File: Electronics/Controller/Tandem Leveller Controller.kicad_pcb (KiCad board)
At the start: 2 copper layers, 212 x 145 mm, 133 parts, among them J1 Conn_01x02, J10 CAN BUS, J11 TRACTOR BATTERY, J12 PWR SWITCH, J13 VALVE POWER, J14 TABLET 1 PWR, J15 TABLET 2 PWR, J16 SLAVE TABLET, J17 MASTER TABLET, J18 292303-7, J19 292303-7, J2 GPS SIM, J20 FRONT HEIGHT, J21 REAR HEIGHT, J23 CAN, J24 CAN BUS, J25 CAN BUS, J3 Conn_01x02, J4 Conn_01x02, J5 Conn_01x02, J6 Conn_01x02, J7 Conn_01x02, J8 Conn_01x02, J9 TERM, U1 TEENSY 4.0, U10 FT232RL, U11 FT232RL, U12 FT232RL, U13 FT232RL, U14 FT232RL, U15 FT232RL, U16 USB2517, U17 MIC2026-1YM, U2 simpleRTK2B, U3 simpleRTK2B, U4 simpleRTK2B, U5 TJA1462ATK-0Z, U6 PESD2CANFD24V-TR, U7 LM2596S-5, U8 LM2587S-ADJ/NOPB, U9 LM2587S-ADJ/NOPB, Y1 FA-238 24.0000MD30X-W5

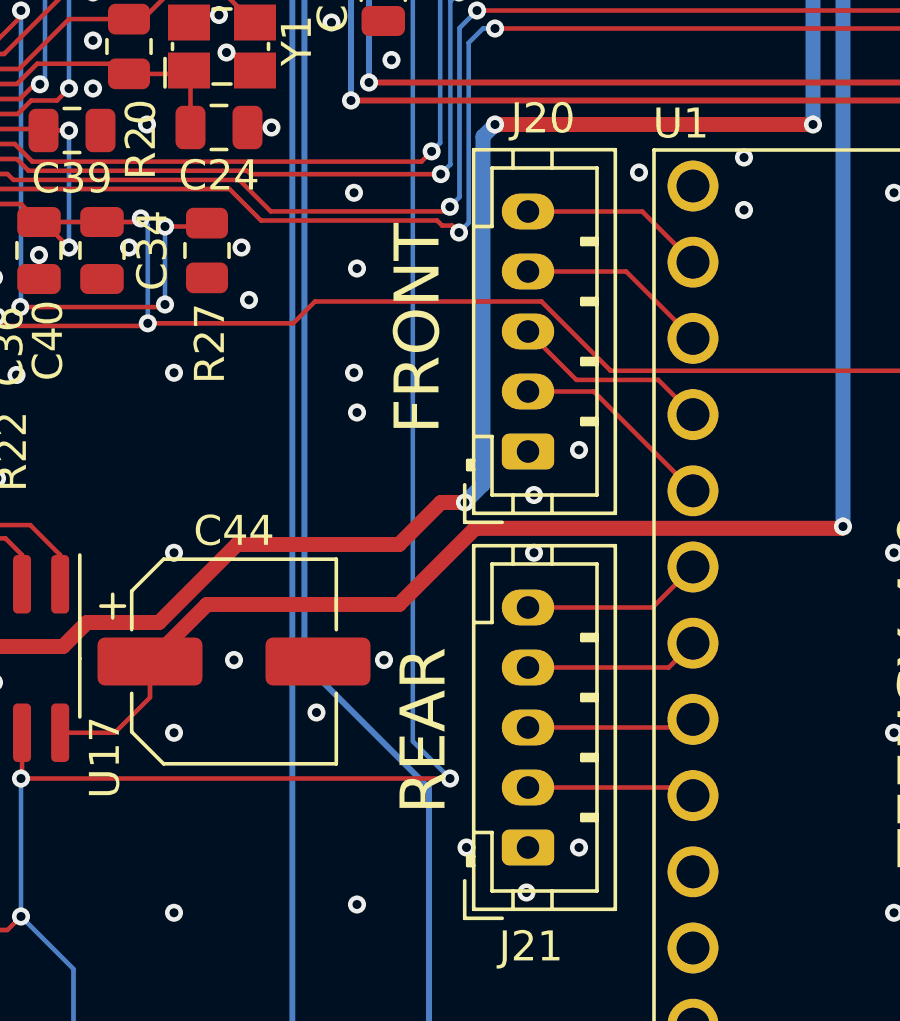
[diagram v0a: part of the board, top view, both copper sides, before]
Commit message: Renamed valve control connectors and reordered pins to match pinout of MDD10A connectors.
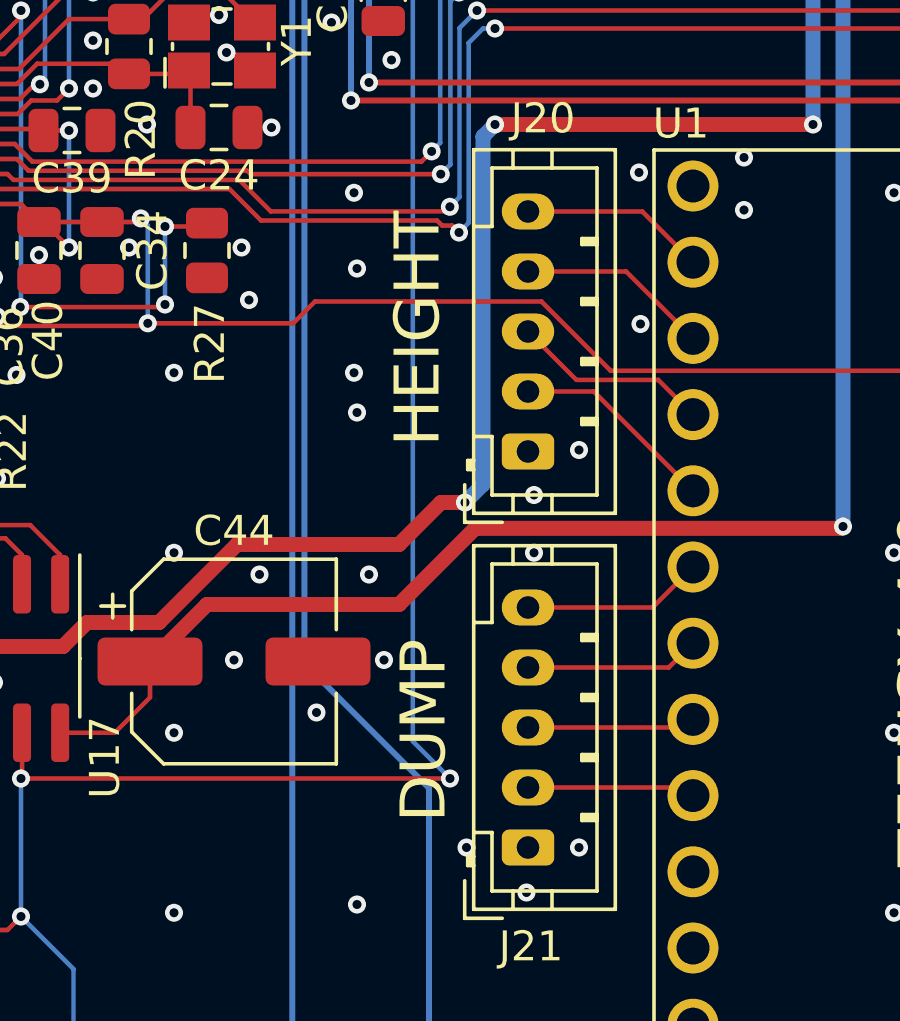
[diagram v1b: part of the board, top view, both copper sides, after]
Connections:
- net /Valve Control/FRONT_DIR1 renamed /Valve Control/FRONT_HEIGHT_PWM
- net /Valve Control/FRONT_DIR2 renamed /Valve Control/REAR_HEIGHT_PWM
- net /Valve Control/FRONT_PWM1 renamed /Valve Control/FRONT_HEIGHT_DIR
- net /Valve Control/FRONT_PWM2 renamed /Valve Control/REAR_HEIGHT_DIR
- net /Valve Control/REAR_DIR1 renamed /Valve Control/FRONT_DUMP_PWM
- net /Valve Control/REAR_DIR2 renamed /Valve Control/REAR_DUMP_PWM
- net /Valve Control/REAR_PWM1 renamed /Valve Control/FRONT_DUMP_DIR
- net /Valve Control/REAR_PWM2 renamed /Valve Control/REAR_DUMP_DIR
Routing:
- net GND: vias 858 -> 861
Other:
- board text added: "DUMP"
- board text added: "HEIGHT"
- board text removed: "FRONT"
- board text removed: "REAR"
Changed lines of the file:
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@@
   (net 63 "Net-(J19-D-)")
   (net 64 "Net-(J19-D+)")
-  (net 65 "/Valve Control/FRONT_PWM2")
-  (net 66 "/Valve Control/FRONT_DIR2")
-  (net 67 "/Valve Control/FRONT_PWM1")
-  (net 68 "/Valve Control/FRONT_DIR1")
-  (net 69 "/Valve Control/REAR_PWM2")
-  (net 70 "/Valve Control/REAR_DIR2")
-  (net 71 "/Valve Control/REAR_PWM1")
-  (net 72 "/Valve Control/REAR_DIR1")
+  (net 65 "/Valve Control/REAR_HEIGHT_DIR")
+  (net 66 "/Valve Control/REAR_HEIGHT_PWM")
+  (net 67 "/Valve Control/FRONT_HEIGHT_DIR")
+  (net 68 "/Valve Control/FRONT_HEIGHT_PWM")
+  (net 69 "/Valve Control/REAR_DUMP_DIR")
+  (net 70 "/Valve Control/REAR_DUMP_PWM")
+  (net 71 "/Valve Control/FRONT_DUMP_DIR")
+  (net 72 "/Valve Control/FRONT_DUMP_PWM")
   (net 73 "unconnected-(U1-GPIO11_MOSI-Pad13)")
   (net 74 "Net-(U5-CANL)")
@@
       (net 2 "GND") (pinfunction "Pin_1") (pintype "passive"))
     (pad "2" thru_hole oval (at 2 0 90) (size 1.2 1.75) (drill 0.75) (layers "*.Cu" "*.Mask")
-      (net 70 "/Valve Control/REAR_DIR2") (pinfunction "Pin_2") (pintype "passive"))
+      (net 70 "/Valve Control/REAR_DUMP_PWM") (pinfunction "Pin_2") (pintype "passive"))
     (pad "3" thru_hole oval (at 4 0 90) (size 1.2 1.75) (drill 0.75) (layers "*.Cu" "*.Mask")
-      (net 69 "/Valve Control/REAR_PWM2") (pinfunction "Pin_3") (pintype "passive"))
+      (net 69 "/Valve Control/REAR_DUMP_DIR") (pinfunction "Pin_3") (pintype "passive"))
     (pad "4" thru_hole oval (at 6 0 90) (size 1.2 1.75) (drill 0.75) (layers "*.Cu" "*.Mask")
-      (net 72 "/Valve Control/REAR_DIR1") (pinfunction "Pin_4") (pintype "passive"))
+      (net 72 "/Valve Control/FRONT_DUMP_PWM") (pinfunction "Pin_4") (pintype "passive"))
     (pad "5" thru_hole oval (at 8 0 90) (size 1.2 1.75) (drill 0.75) (layers "*.Cu" "*.Mask")
-      (net 71 "/Valve Control/REAR_PWM1") (pinfunction "Pin_5") (pintype "passive"))
+      (net 71 "/Valve Control/FRONT_DUMP_DIR") (pinfunction "Pin_5") (pintype "passive"))
     (model "${KICAD6_3DMODEL_DIR}/Connector_JST.3dshapes/JST_PH_B5B-PH-K_1x05_P2.00mm_Vertical.wrl"
       (offset (xyz 0 0 0))
@@
       (net 2 "GND") (pinfunction "Pin_1") (pintype "passive"))
     (pad "2" thru_hole oval (at 2 0 90) (size 1.2 1.75) (drill 0.75) (layers "*.Cu" "*.Mask")
-      (net 66 "/Valve Control/FRONT_DIR2") (pinfunction "Pin_2") (pintype "passive"))
+      (net 66 "/Valve Control/REAR_HEIGHT_PWM") (pinfunction "Pin_2") (pintype "passive"))
     (pad "3" thru_hole oval (at 4 0 90) (size 1.2 1.75) (drill 0.75) (layers "*.Cu" "*.Mask")
-      (net 65 "/Valve Control/FRONT_PWM2") (pinfunction "Pin_3") (pintype "passive"))
+      (net 65 "/Valve Control/REAR_HEIGHT_DIR") (pinfunction "Pin_3") (pintype "passive"))
     (pad "4" thru_hole oval (at 6 0 90) (size 1.2 1.75) (drill 0.75) (layers "*.Cu" "*.Mask")
-      (net 68 "/Valve Control/FRONT_DIR1") (pinfunction "Pin_4") (pintype "passive"))
+      (net 68 "/Valve Control/FRONT_HEIGHT_PWM") (pinfunction "Pin_4") (pintype "passive"))
     (pad "5" thru_hole oval (at 8 0 90) (size 1.2 1.75) (drill 0.75) (layers "*.Cu" "*.Mask")
-      (net 67 "/Valve Control/FRONT_PWM1") (pinfunction "Pin_5") (pintype "passive"))
+      (net 67 "/Valve Control/FRONT_HEIGHT_DIR") (pinfunction "Pin_5") (pintype "passive"))
     (model "${KICAD6_3DMODEL_DIR}/Connector_JST.3dshapes/JST_PH_B5B-PH-K_1x05_P2.00mm_Vertical.wrl"
       (offset (xyz 0 0 0))
@@
       (net 2 "GND") (pinfunction "GND") (pintype "power_in"))
     (pad "2" thru_hole circle (at 0 2.54) (size 1.7 1.7) (drill 1.1) (layers "*.Cu" "*.Mask")
-      (net 67 "/Valve Control/FRONT_PWM1") (pinfunction "GPIO0_CRX2_RX1") (pintype "passive"))
+      (net 67 "/Valve Control/FRONT_HEIGHT_DIR") (pinfunction "GPIO0_CRX2_RX1") (pintype "passive"))
     (pad "3" thru_hole circle (at 0 5.08) (size 1.7 1.7) (drill 1.1) (layers "*.Cu" "*.Mask")
-      (net 68 "/Valve Control/FRONT_DIR1") (pinfunction "GPIO1_CTX2_TX1") (pintype "passive"))
+      (net 68 "/Valve Control/FRONT_HEIGHT_PWM") (pinfunction "GPIO1_CTX2_TX1") (pintype "passive"))
     (pad "4" thru_hole circle (at 0 7.62) (size 1.7 1.7) (drill 1.1) (layers "*.Cu" "*.Mask")
-      (net 65 "/Valve Control/FRONT_PWM2") (pinfunction "GPIO2") (pintype "passive"))
+      (net 65 "/Valve Control/REAR_HEIGHT_DIR") (pinfunction "GPIO2") (pintype "passive"))
     (pad "5" thru_hole circle (at 0 10.16) (size 1.7 1.7) (drill 1.1) (layers "*.Cu" "*.Mask")
-      (net 66 "/Valve Control/FRONT_DIR2") (pinfunction "GPIO3") (pintype "passive"))
+      (net 66 "/Valve Control/REAR_HEIGHT_PWM") (pinfunction "GPIO3") (pintype "passive"))
     (pad "6" thru_hole circle (at 0 12.7) (size 1.7 1.7) (drill 1.1) (layers "*.Cu" "*.Mask")
-      (net 71 "/Valve Control/REAR_PWM1") (pinfunction "GPIO4") (pintype "passive"))
+      (net 71 "/Valve Control/FRONT_DUMP_DIR") (pinfunction "GPIO4") (pintype "passive"))
     (pad "7" thru_hole circle (at 0 15.24) (size 1.7 1.7) (drill 1.1) (layers "*.Cu" "*.Mask")
-      (net 72 "/Valve Control/REAR_DIR1") (pinfunction "GPIO5") (pintype "passive"))
+      (net 72 "/Valve Control/FRONT_DUMP_PWM") (pinfunction "GPIO5") (pintype "passive"))
     (pad "8" thru_hole circle (at 0 17.78) (size 1.7 1.7) (drill 1.1) (layers "*.Cu" "*.Mask")
-      (net 69 "/Valve Control/REAR_PWM2") (pinfunction "GPIO6") (pintype "passive"))
+      (net 69 "/Valve Control/REAR_DUMP_DIR") (pinfunction "GPIO6") (pintype "passive"))
     (pad "9" thru_hole circle (at 0 20.32) (size 1.7 1.7) (drill 1.1) (layers "*.Cu" "*.Mask")
-      (net 70 "/Valve Control/REAR_DIR2") (pinfunction "GPIO7_RX2") (pintype "passive"))
+      (net 70 "/Valve Control/REAR_DUMP_PWM") (pinfunction "GPIO7_RX2") (pintype "passive"))
     (pad "10" thru_hole circle (at 0 22.86) (size 1.7 1.7) (drill 1.1) (layers "*.Cu" "*.Mask")
       (net 32 "unconnected-(U1-GPIO8_TX2-Pad10)") (pinfunction "GPIO8_TX2") (pintype "passive+no_connect"))
@@
     (effects (font (size 1.5 1.5) (thickness 0.2)) (justify left bottom))
   )
-  (gr_text "FRONT" (at 194.5 62.2 90) (layer "F.SilkS")
+  (gr_text "HEIGHT" (at 194.5 62.2 90) (layer "F.SilkS")
     (effects (font (size 1.5 1.5) (thickness 0.2)) (justify bottom))
   )
@@
     (effects (font (size 1.5 1.5) (thickness 0.2)) (justify left bottom))
   )
-  (gr_text "REAR" (at 194.7 75.6 90) (layer "F.SilkS")
+  (gr_text "DUMP" (at 194.7 75.6 90) (layer "F.SilkS")
     (effects (font (size 1.5 1.5) (thickness 0.2)) (justify bottom))
   )
@@
   (via (at 143.5 69.675) (size 0.6) (drill 0.3) (layers "F.Cu" "B.Cu") (free) (net 2))
   (via (at 113.5 93.675) (size 0.6) (drill 0.3) (layers "F.Cu" "B.Cu") (free) (net 2))
+  (via (at 192 70.4) (size 0.6) (drill 0.3) (layers "F.Cu" "B.Cu") (free) (net 2))
   (via (at 83.5 117.675) (size 0.6) (drill 0.3) (layers "F.Cu" "B.Cu") (free) (net 2))
   (via (at 233.5 51.675) (size 0.6) (drill 0.3) (layers "F.Cu" "B.Cu") (free) (net 2))
@@
   (via (at 101.5 129.675) (size 0.6) (drill 0.3) (layers "F.Cu" "B.Cu") (free) (net 2))
   (via (at 168 148) (size 0.6) (drill 0.3) (layers "F.Cu" "B.Cu") (free) (net 2))
+  (via (at 201.05 62.05) (size 0.6) (drill 0.3) (layers "F.Cu" "B.Cu") (free) (net 2))
   (via (at 143.5 117.675) (size 0.6) (drill 0.3) (layers "F.Cu" "B.Cu") (free) (net 2))
   (via (at 185.5 123.675) (size 0.6) (drill 0.3) (layers "F.Cu" "B.Cu") (free) (net 2))
@@
   (via (at 197.5 135.675) (size 0.6) (drill 0.3) (layers "F.Cu" "B.Cu") (free) (net 2))
   (via (at 161.75 27.25) (size 0.6) (drill 0.3) (layers "F.Cu" "B.Cu") (free) (net 2))
+  (via (at 188.35 70.4) (size 0.6) (drill 0.3) (layers "F.Cu" "B.Cu") (free) (net 2))
   (via (at 89.5 93.675) (size 0.6) (drill 0.3) (layers "F.Cu" "B.Cu") (free) (net 2))
   (segment (start 104.7 66.35) (end 124.7 66.35) (width 1.4) (layer "F.Cu") (net 3))

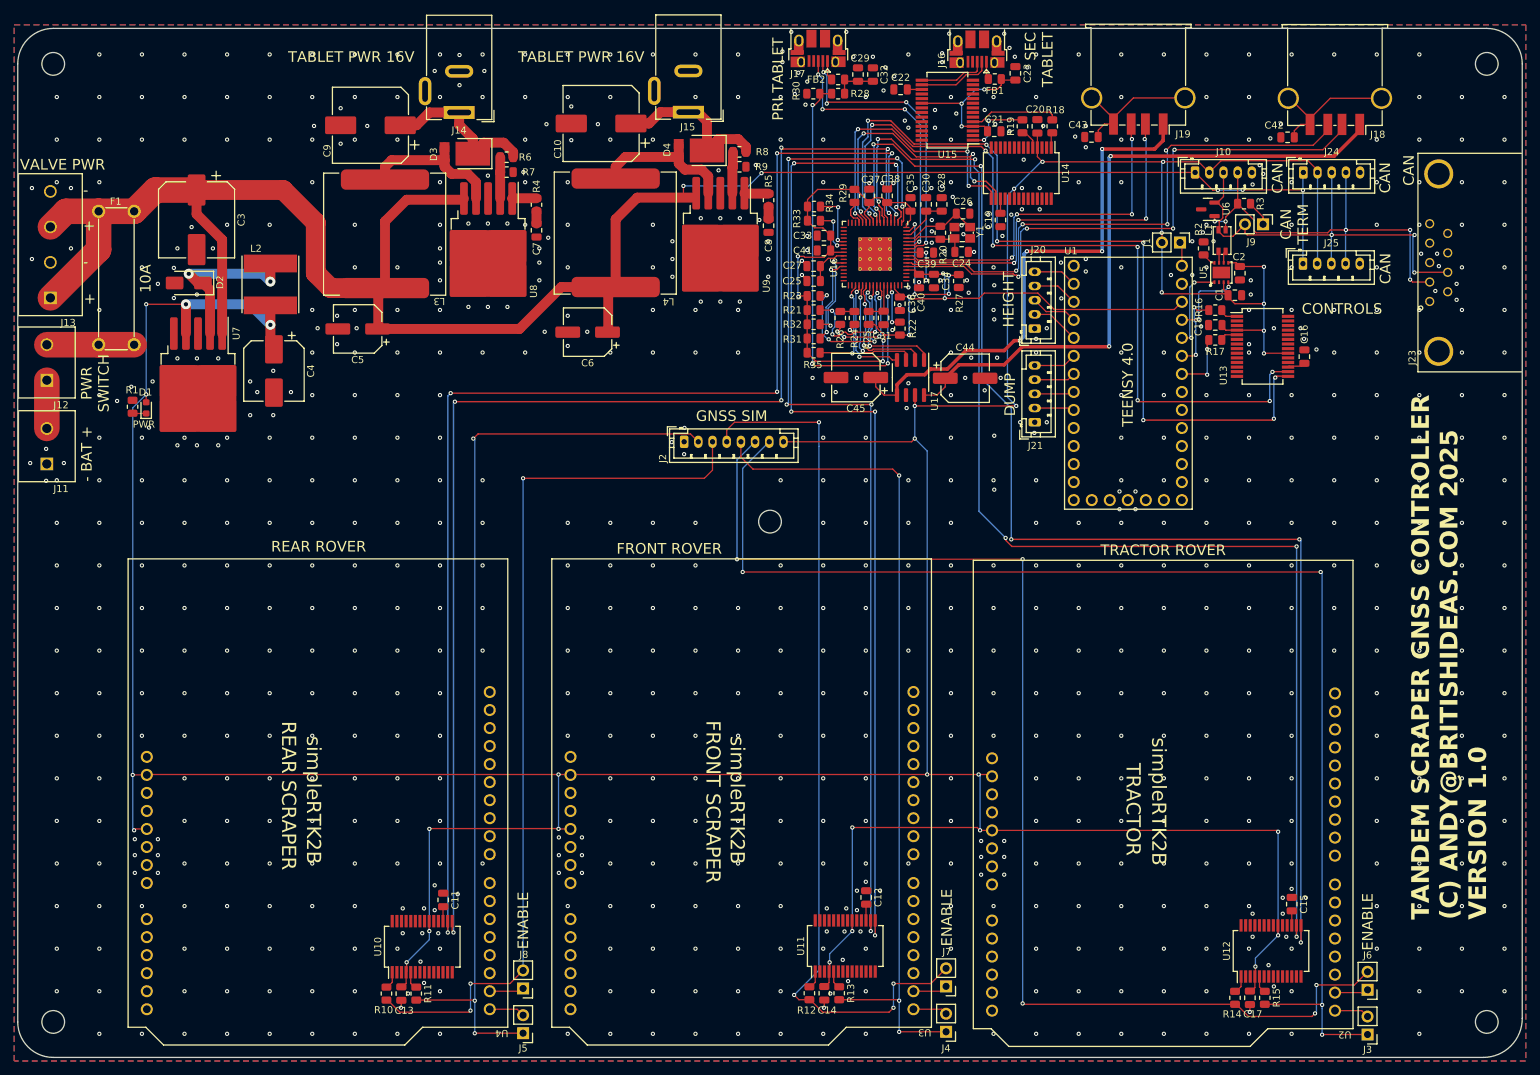
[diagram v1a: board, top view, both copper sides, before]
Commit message: Increased 5V and 12V track thickness to CAN connnectors on controller board.
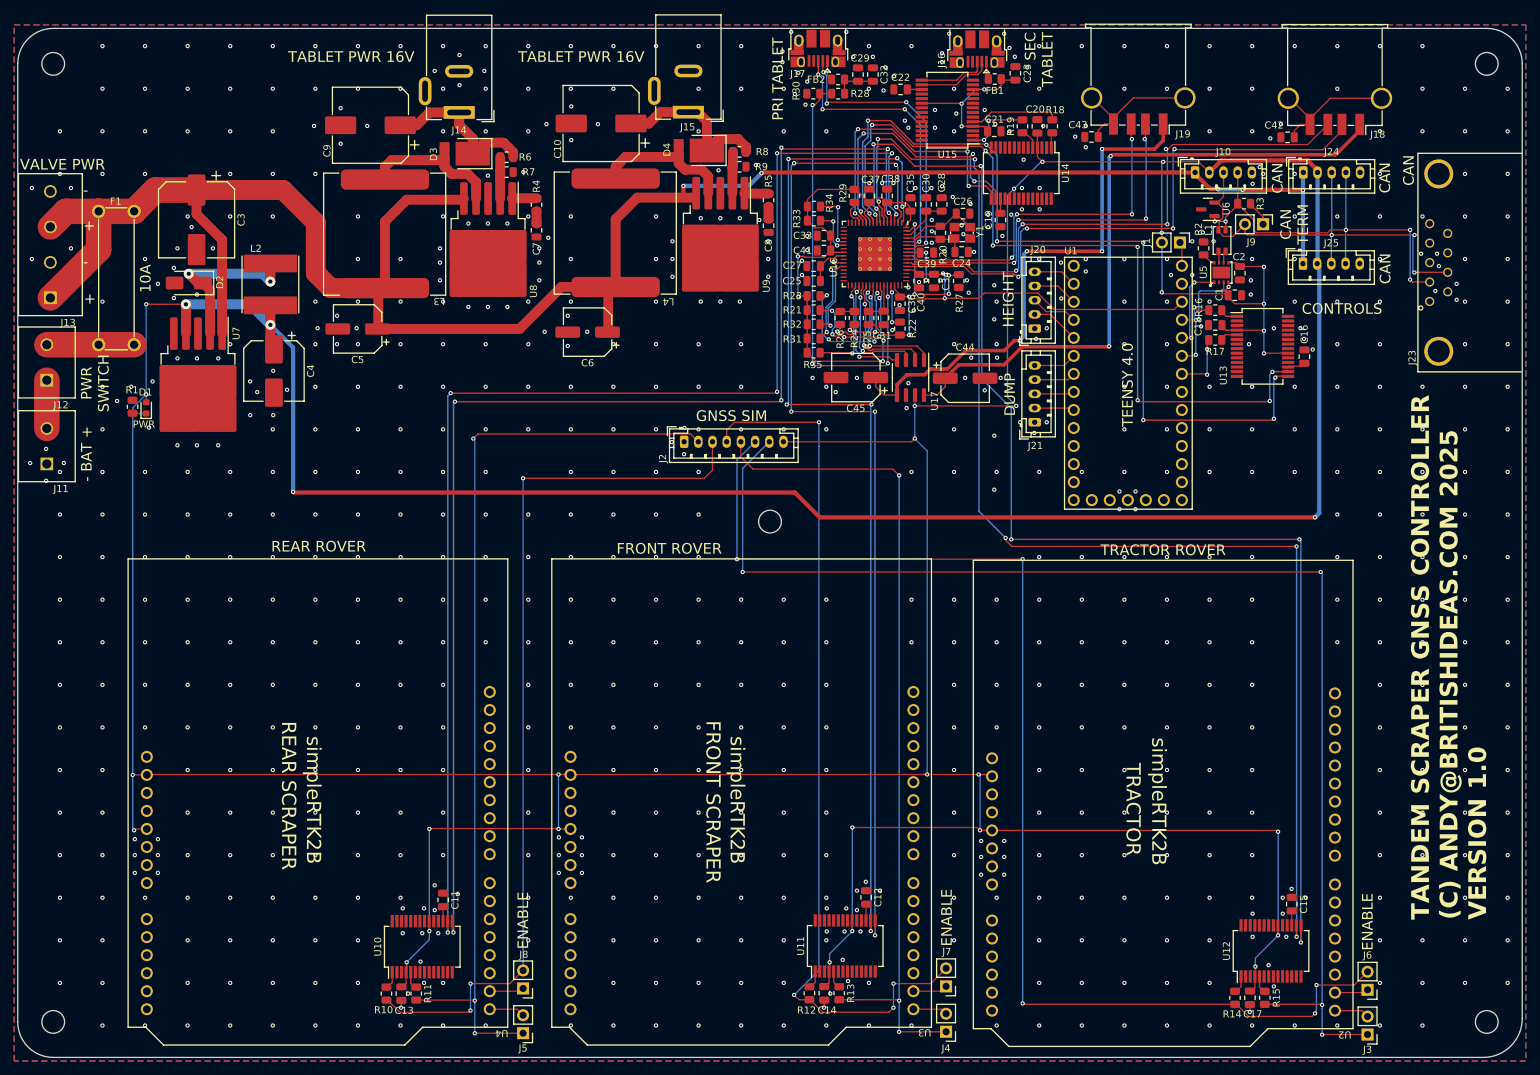
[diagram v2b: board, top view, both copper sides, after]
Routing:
- net +5V: track 647.8 -> 854.4 mm, vias 32 -> 34
- net GND: vias 861 -> 845
